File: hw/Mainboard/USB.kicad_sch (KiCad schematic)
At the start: 8 parts, among them J25 USB2.0_HOST_TYPE_C

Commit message: hw: 25x2 header (wip)
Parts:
- renumbered J25 to J26
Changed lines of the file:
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@@
   (symbol (lib_id "PET:PD_GND") (at 102.87 88.9 0) (unit 1)
     (in_bom yes) (on_board yes) (fields_autoplaced)
-    (property "Reference" "#PWR0150" (id 0) (at 102.87 95.25 0)
+    (property "Reference" "#PWR0152" (id 0) (at 102.87 95.25 0)
       (effects (font (size 1.27 1.27)) hide)
     )
@@
   (symbol (lib_id "JLCPCB:USB_C_Receptacle_USB2.0") (at 152.4 92.71 0) (mirror y) (unit 1)
     (in_bom yes) (on_board yes) (fields_autoplaced)
-    (property "Reference" "J25" (id 0) (at 163.83 90.8049 0)
+    (property "Reference" "J26" (id 0) (at 163.83 90.8049 0)
       (effects (font (size 1.27 1.27)) (justify right))
     )
@@
   (symbol (lib_id "power:+5V") (at 102.87 74.93 0) (mirror y) (unit 1)
     (in_bom yes) (on_board yes) (fields_autoplaced)
-    (property "Reference" "#PWR0149" (id 0) (at 102.87 78.74 0)
+    (property "Reference" "#PWR0151" (id 0) (at 102.87 78.74 0)
       (effects (font (size 1.27 1.27)) hide)
     )
@@
   (symbol (lib_id "PET:PD_GND") (at 153.67 123.19 0) (unit 1)
     (in_bom yes) (on_board yes) (fields_autoplaced)
-    (property "Reference" "#PWR0151" (id 0) (at 153.67 129.54 0)
+    (property "Reference" "#PWR0153" (id 0) (at 153.67 129.54 0)
       (effects (font (size 1.27 1.27)) hide)
     )
@@
   (symbol (lib_id "power:GND") (at 160.02 123.19 0) (unit 1)
     (in_bom yes) (on_board yes) (fields_autoplaced)
-    (property "Reference" "#PWR0152" (id 0) (at 160.02 129.54 0)
+    (property "Reference" "#PWR0154" (id 0) (at 160.02 129.54 0)
       (effects (font (size 1.27 1.27)) hide)
     )

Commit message: hw: 2x config switch (wip)
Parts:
- renumbered J26 to J25
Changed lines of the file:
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@@
   (symbol (lib_id "PET:PD_GND") (at 102.87 88.9 0) (unit 1)
     (in_bom yes) (on_board yes) (fields_autoplaced)
-    (property "Reference" "#PWR0152" (id 0) (at 102.87 95.25 0)
+    (property "Reference" "#PWR0158" (id 0) (at 102.87 95.25 0)
       (effects (font (size 1.27 1.27)) hide)
     )
@@
   (symbol (lib_id "JLCPCB:USB_C_Receptacle_USB2.0") (at 152.4 92.71 0) (mirror y) (unit 1)
     (in_bom yes) (on_board yes) (fields_autoplaced)
-    (property "Reference" "J26" (id 0) (at 163.83 90.8049 0)
+    (property "Reference" "J25" (id 0) (at 163.83 90.8049 0)
       (effects (font (size 1.27 1.27)) (justify right))
     )
@@
   (symbol (lib_id "power:+5V") (at 102.87 74.93 0) (mirror y) (unit 1)
     (in_bom yes) (on_board yes) (fields_autoplaced)
-    (property "Reference" "#PWR0151" (id 0) (at 102.87 78.74 0)
+    (property "Reference" "#PWR0157" (id 0) (at 102.87 78.74 0)
       (effects (font (size 1.27 1.27)) hide)
     )
@@
   (symbol (lib_id "PET:PD_GND") (at 153.67 123.19 0) (unit 1)
     (in_bom yes) (on_board yes) (fields_autoplaced)
-    (property "Reference" "#PWR0153" (id 0) (at 153.67 129.54 0)
+    (property "Reference" "#PWR0159" (id 0) (at 153.67 129.54 0)
       (effects (font (size 1.27 1.27)) hide)
     )
@@
   (symbol (lib_id "power:GND") (at 160.02 123.19 0) (unit 1)
     (in_bom yes) (on_board yes) (fields_autoplaced)
-    (property "Reference" "#PWR0154" (id 0) (at 160.02 129.54 0)
+    (property "Reference" "#PWR0160" (id 0) (at 160.02 129.54 0)
       (effects (font (size 1.27 1.27)) hide)
     )

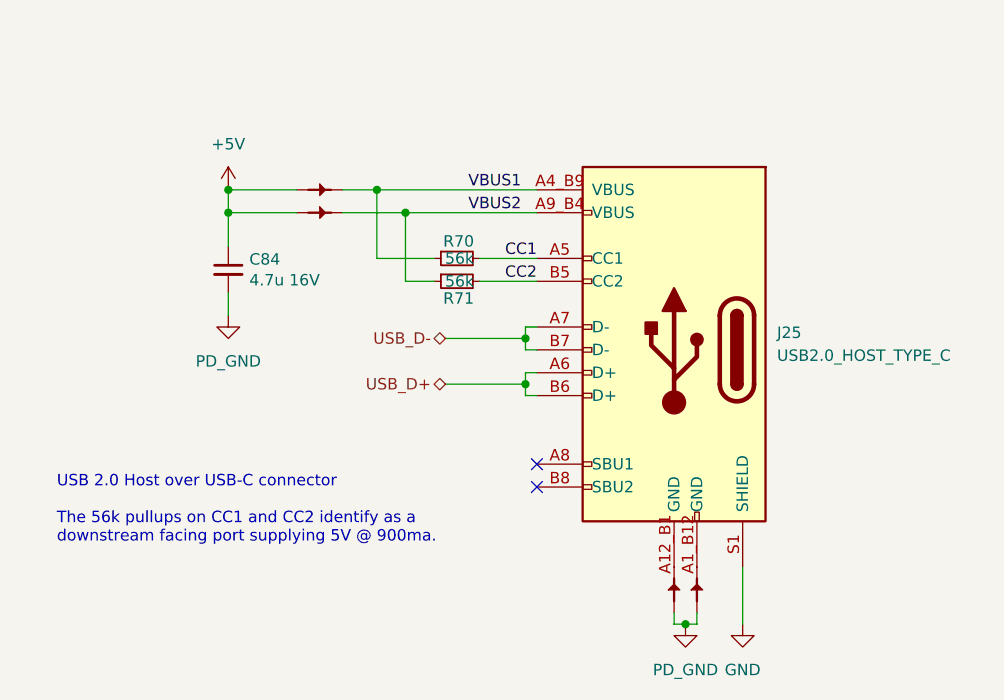
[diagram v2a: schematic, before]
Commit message: hw: add vbus diode, just starting fills
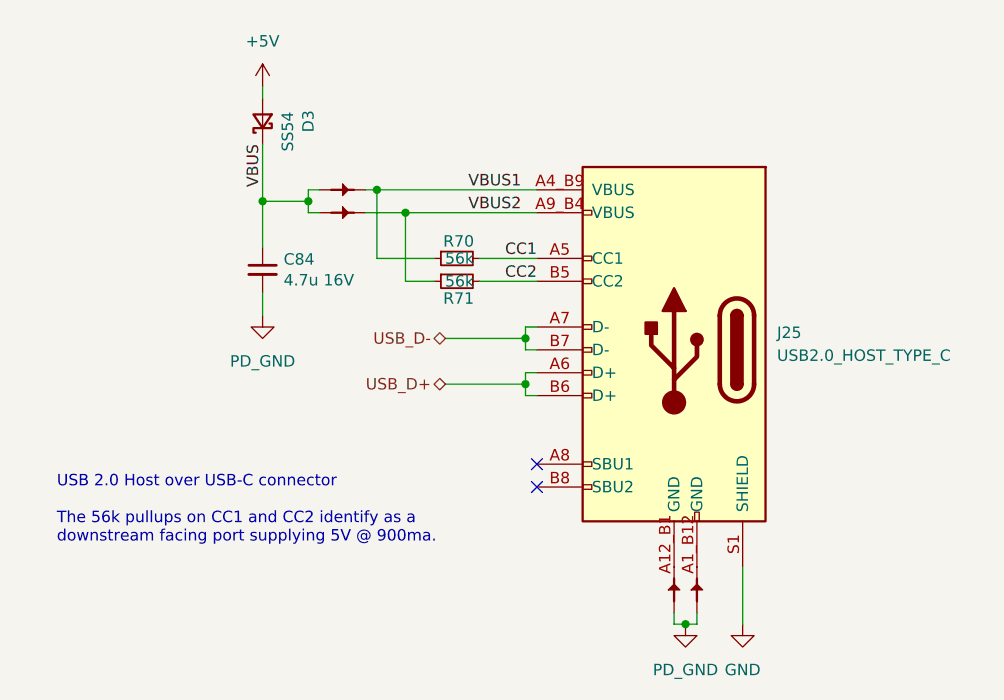
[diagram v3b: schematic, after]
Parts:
- added D3: SS54, Diode_SMD:D_SMA, symbol Device:D_Schottky_Small
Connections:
- net +5V: now also D3.2 (A); no longer C84.1, PT51.1, PT52.1
- new net VBUS: C84.1, D3.1 (K), PT51.1, PT52.1
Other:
- moved on the sheet: C84

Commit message: hw: remove series termination, gnd under hdmi (wip)
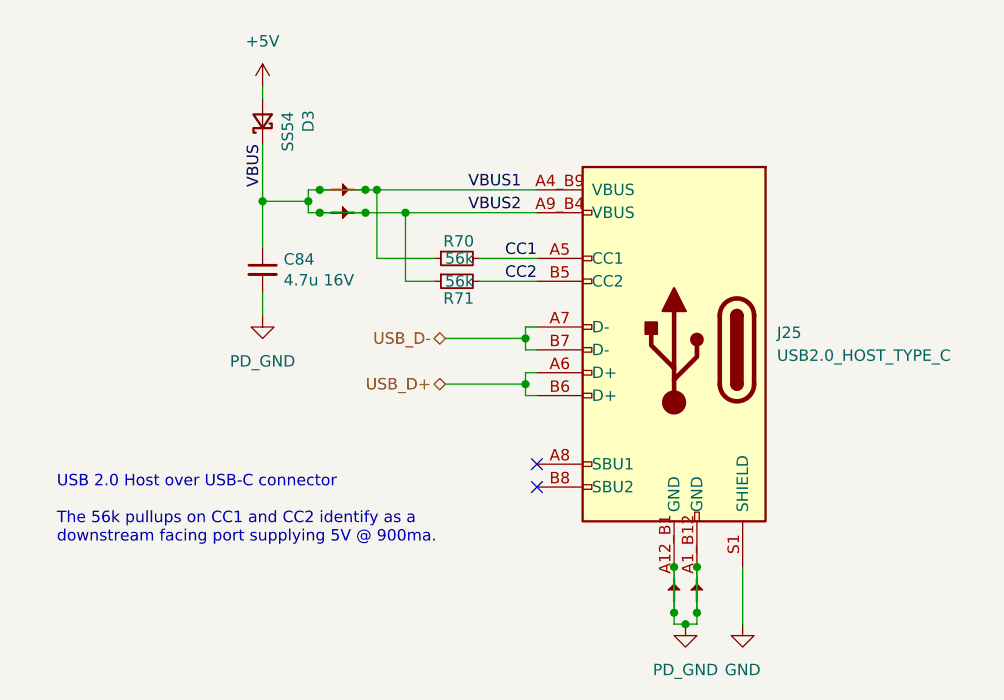
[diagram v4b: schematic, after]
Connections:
- net VBUS1 is gone; now on net VBUS: J25.A4_B9 (VBUS), PT51.2, R70.1
- net VBUS2 is gone; now on net VBUS: J25.A9_B4 (VBUS), PT52.2, R71.1
- net PD_GND: now also J25.A12_B1 (GND), J25.A1_B12 (GND), PT53.2, PT54.2
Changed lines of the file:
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@@
     (title "CBM PET Mainboard Replacement")
   )
+  (junction (at 152.4 116.84) (diameter 0) (color 0 0 0 0)
+  )
+  (junction (at 118.11 74.93) (diameter 0) (color 0 0 0 0)
+  )
+  (junction (at 152.4 121.92) (diameter 0) (color 0 0 0 0)
+  )
   (junction (at 153.67 123.19) (diameter 0) (color 0 0 0 0)
+  )
+  (junction (at 118.11 77.47) (diameter 0) (color 0 0 0 0)
+  )
+  (junction (at 154.94 116.84) (diameter 0) (color 0 0 0 0)
   )
   (junction (at 135.89 96.52) (diameter 0) (color 0 0 0 0)
@@
   (junction (at 135.89 91.44) (diameter 0) (color 0 0 0 0)
   )
+  (junction (at 113.03 74.93) (diameter 0) (color 0 0 0 0)
+  )
+  (junction (at 154.94 121.92) (diameter 0) (color 0 0 0 0)
+  )
   (junction (at 122.555 77.47) (diameter 0) (color 0 0 0 0)
+  )
+  (junction (at 113.03 77.47) (diameter 0) (color 0 0 0 0)
   )
   (no_connect (at 137.16 105.41))
@@
     (stroke (width 0) (type default) (color 0 0 0 0))
   )
+  (wire (pts (xy 154.94 116.84) (xy 154.94 121.92))
+    (stroke (width 0) (type default) (color 0 0 0 0))
+  )
   (wire (pts (xy 152.4 121.92) (xy 152.4 123.19))
     (stroke (width 0) (type default) (color 0 0 0 0))
@@
     (stroke (width 0) (type default) (color 0 0 0 0))
   )
+  (wire (pts (xy 113.03 77.47) (xy 118.11 77.47))
+    (stroke (width 0) (type default) (color 0 0 0 0))
+  )
   (wire (pts (xy 118.11 77.47) (xy 122.555 77.47))
     (stroke (width 0) (type default) (color 0 0 0 0))
   )
   (wire (pts (xy 119.38 74.93) (xy 137.16 74.93))
+    (stroke (width 0) (type default) (color 0 0 0 0))
+  )
+  (wire (pts (xy 113.03 74.93) (xy 118.11 74.93))
     (stroke (width 0) (type default) (color 0 0 0 0))
   )
@@
     (stroke (width 0) (type default) (color 0 0 0 0))
   )
+  (wire (pts (xy 152.4 116.84) (xy 152.4 121.92))
+    (stroke (width 0) (type default) (color 0 0 0 0))
+  )

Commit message: hw: caps & logos (wip)
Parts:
- added C101: 47u 10V, Capacitor_SMD:C_1206_3216Metric, symbol Device:C_Small
- C84: value 4.7u 16V -> 1u; footprint Capacitor_SMD:C_0603_1608Metric -> Capacitor_SMD:C_0402_1005Metric; LCSC C19666 -> C52923
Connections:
- net PD_GND: now also C101.2
- net VBUS: now also C101.1
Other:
- title: CBM PET Mainboard Replacement -> EconoPET 40/8096
- moved on the sheet: D3

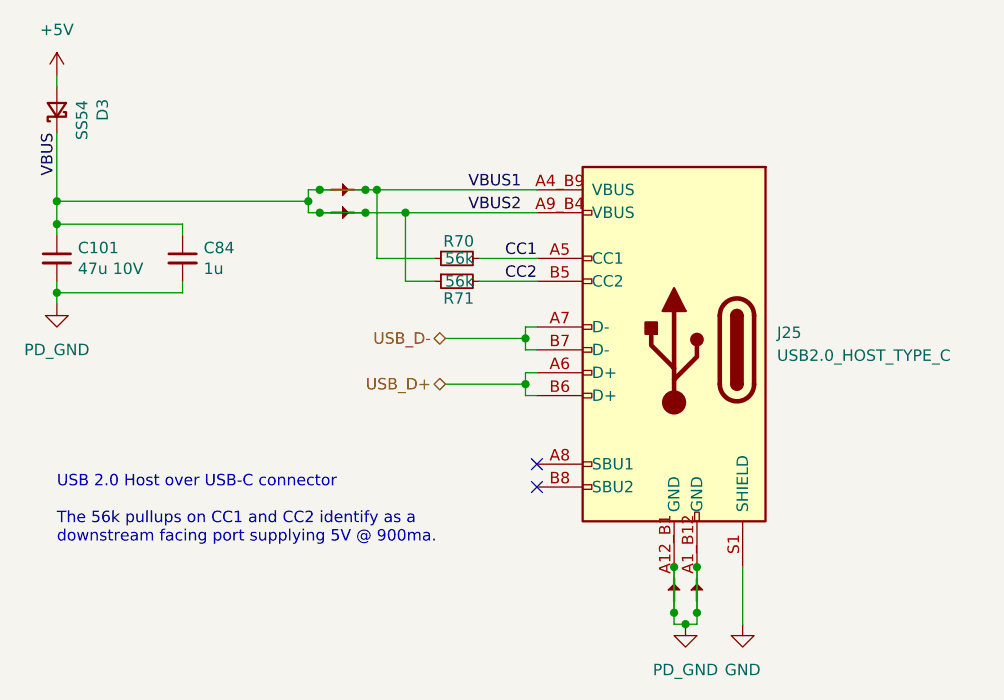
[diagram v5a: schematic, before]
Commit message: hw: remove net/power ties
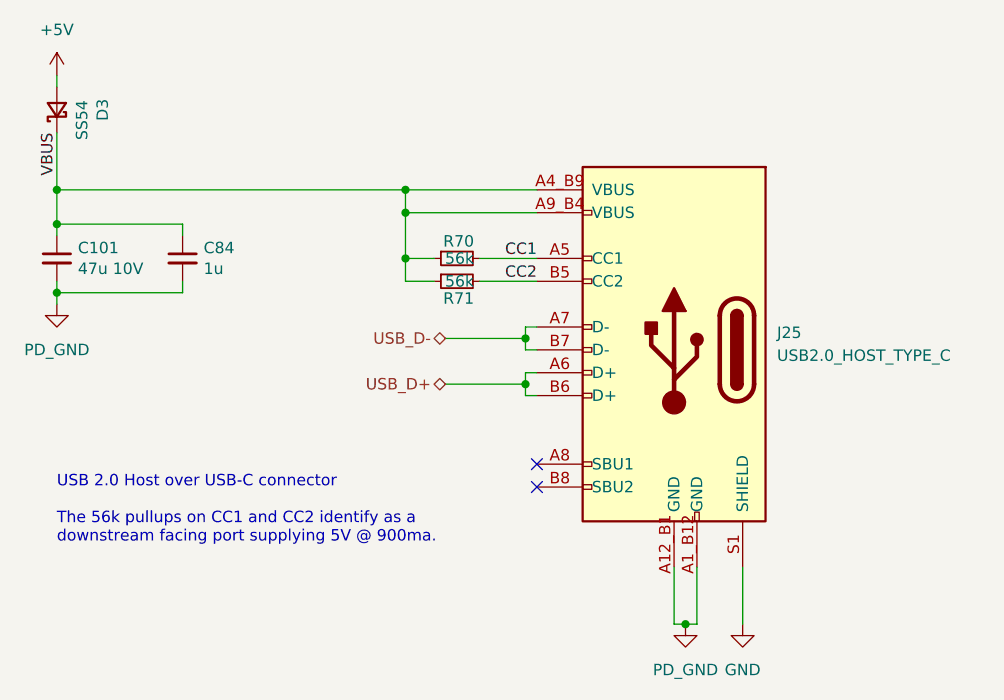
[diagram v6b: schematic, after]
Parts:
- removed PT51, PT52, PT53, PT54: PowerTie_2, PET:NetTie-2_SMD_Pad_1.6_to_0.4mm, symbol PET:PowerTie_2
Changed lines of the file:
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@@
     (rev "A")
   )
-  (junction (at 152.4 116.84) (diameter 0) (color 0 0 0 0)
-  )
-  (junction (at 118.11 74.93) (diameter 0) (color 0 0 0 0)
-  )
-  (junction (at 152.4 121.92) (diameter 0) (color 0 0 0 0)
-  )
   (junction (at 153.67 123.19) (diameter 0) (color 0 0 0 0)
   )
-  (junction (at 118.11 77.47) (diameter 0) (color 0 0 0 0)
+  (junction (at 122.555 77.47) (diameter 0) (color 0 0 0 0)
   )
   (junction (at 83.82 78.74) (diameter 0) (color 0 0 0 0)
   )
-  (junction (at 154.94 116.84) (diameter 0) (color 0 0 0 0)
+  (junction (at 83.82 74.93) (diameter 0) (color 0 0 0 0)
   )
   (junction (at 83.82 86.36) (diameter 0) (color 0 0 0 0)
@@
   (junction (at 135.89 96.52) (diameter 0) (color 0 0 0 0)
   )
-  (junction (at 119.38 74.93) (diameter 0) (color 0 0 0 0)
-  )
-  (junction (at 111.76 76.2) (diameter 0) (color 0 0 0 0)
-  )
   (junction (at 135.89 91.44) (diameter 0) (color 0 0 0 0)
   )
-  (junction (at 113.03 74.93) (diameter 0) (color 0 0 0 0)
-  )
-  (junction (at 83.82 76.2) (diameter 0) (color 0 0 0 0)
-  )
-  (junction (at 154.94 121.92) (diameter 0) (color 0 0 0 0)
-  )
-  (junction (at 122.555 77.47) (diameter 0) (color 0 0 0 0)
-  )
-  (junction (at 113.03 77.47) (diameter 0) (color 0 0 0 0)
+  (junction (at 122.555 82.55) (diameter 0) (color 0 0 0 0)
+  )
+  (junction (at 122.555 74.93) (diameter 0) (color 0 0 0 0)
   )
   (no_connect (at 137.16 105.41))
   (no_connect (at 137.16 107.95))
+  (wire (pts (xy 83.82 74.93) (xy 83.82 78.74))
+    (stroke (width 0) (type default) (color 0 0 0 0))
+  )
   (wire (pts (xy 83.82 78.74) (xy 97.79 78.74))
     (stroke (width 0) (type default) (color 0 0 0 0))
@@
     (stroke (width 0) (type default) (color 0 0 0 0))
   )
-  (wire (pts (xy 119.38 82.55) (xy 119.38 74.93))
-    (stroke (width 0) (type default) (color 0 0 0 0))
-  )
   (wire (pts (xy 122.555 77.47) (xy 137.16 77.47))
     (stroke (width 0) (type default) (color 0 0 0 0))
   )
-  (wire (pts (xy 83.82 68.58) (xy 83.82 76.2))
+  (wire (pts (xy 83.82 68.58) (xy 83.82 74.93))
     (stroke (width 0) (type default) (color 0 0 0 0))
   )
@@
     (stroke (width 0) (type default) (color 0 0 0 0))
   )
-  (wire (pts (xy 125.73 82.55) (xy 119.38 82.55))
-    (stroke (width 0) (type default) (color 0 0 0 0))
-  )
   (wire (pts (xy 83.82 62.23) (xy 83.82 63.5))
     (stroke (width 0) (type default) (color 0 0 0 0))
@@
     (stroke (width 0) (type default) (color 0 0 0 0))
   )
-  (wire (pts (xy 154.94 116.84) (xy 154.94 121.92))
-    (stroke (width 0) (type default) (color 0 0 0 0))
-  )
-  (wire (pts (xy 152.4 121.92) (xy 152.4 123.19))
+  (wire (pts (xy 154.94 116.84) (xy 154.94 123.19))
+    (stroke (width 0) (type default) (color 0 0 0 0))
+  )
+  (wire (pts (xy 122.555 82.55) (xy 122.555 77.47))
     (stroke (width 0) (type default) (color 0 0 0 0))
   )
@@
     (stroke (width 0) (type default) (color 0 0 0 0))
   )
-  (wire (pts (xy 113.03 74.93) (xy 111.76 74.93))
+  (wire (pts (xy 83.82 74.93) (xy 122.555 74.93))
     (stroke (width 0) (type default) (color 0 0 0 0))
   )
@@
     (stroke (width 0) (type default) (color 0 0 0 0))
   )
-  (wire (pts (xy 122.555 85.09) (xy 122.555 77.47))
-    (stroke (width 0) (type default) (color 0 0 0 0))
-  )
-  (wire (pts (xy 113.03 77.47) (xy 118.11 77.47))
-    (stroke (width 0) (type default) (color 0 0 0 0))
-  )
-  (wire (pts (xy 118.11 77.47) (xy 122.555 77.47))
-    (stroke (width 0) (type default) (color 0 0 0 0))
-  )
-  (wire (pts (xy 119.38 74.93) (xy 137.16 74.93))
-    (stroke (width 0) (type default) (color 0 0 0 0))
-  )
-  (wire (pts (xy 113.03 74.93) (xy 118.11 74.93))
-    (stroke (width 0) (type default) (color 0 0 0 0))
-  )
-  (wire (pts (xy 111.76 77.47) (xy 113.03 77.47))
+  (wire (pts (xy 122.555 85.09) (xy 122.555 82.55))
+    (stroke (width 0) (type default) (color 0 0 0 0))
+  )
+  (wire (pts (xy 122.555 82.55) (xy 125.73 82.55))
     (stroke (width 0) (type default) (color 0 0 0 0))
   )
@@
     (stroke (width 0) (type default) (color 0 0 0 0))
   )
-  (wire (pts (xy 83.82 76.2) (xy 83.82 78.74))
-    (stroke (width 0) (type default) (color 0 0 0 0))
-  )
-  (wire (pts (xy 111.76 76.2) (xy 111.76 77.47))
-    (stroke (width 0) (type default) (color 0 0 0 0))
-  )
   (wire (pts (xy 135.89 96.52) (xy 127 96.52))
     (stroke (width 0) (type default) (color 0 0 0 0))
@@
     (stroke (width 0) (type default) (color 0 0 0 0))
   )
-  (wire (pts (xy 152.4 116.84) (xy 152.4 121.92))
+  (wire (pts (xy 122.555 77.47) (xy 122.555 74.93))
+    (stroke (width 0) (type default) (color 0 0 0 0))
+  )
+  (wire (pts (xy 152.4 116.84) (xy 152.4 123.19))
     (stroke (width 0) (type default) (color 0 0 0 0))
   )
@@
     (stroke (width 0) (type default) (color 0 0 0 0))
   )
-  (wire (pts (xy 154.94 121.92) (xy 154.94 123.19))
-    (stroke (width 0) (type default) (color 0 0 0 0))
-  )
   (wire (pts (xy 135.89 95.25) (xy 135.89 96.52))
     (stroke (width 0) (type default) (color 0 0 0 0))
@@
     (stroke (width 0) (type default) (color 0 0 0 0))
   )
+  (wire (pts (xy 122.555 74.93) (xy 137.16 74.93))
+    (stroke (width 0) (type default) (color 0 0 0 0))
+  )
   (wire (pts (xy 153.67 123.19) (xy 154.94 123.19))
     (stroke (width 0) (type default) (color 0 0 0 0))
   )
-  (wire (pts (xy 111.76 74.93) (xy 111.76 76.2))
-    (stroke (width 0) (type default) (color 0 0 0 0))
-  )
-  (wire (pts (xy 83.82 76.2) (xy 111.76 76.2))
-    (stroke (width 0) (type default) (color 0 0 0 0))
-  )
   (wire (pts (xy 135.89 91.44) (xy 135.89 92.71))
     (stroke (width 0) (type default) (color 0 0 0 0))
   )
   (wire (pts (xy 97.79 80.01) (xy 97.79 78.74))
-    (stroke (width 0) (type default) (color 0 0 0 0))
-  )
-  (wire (pts (xy 118.11 74.93) (xy 119.38 74.93))
     (stroke (width 0) (type default) (color 0 0 0 0))
   )
@@
     (effects (font (size 1.27 1.27)) (justify left bottom))
   )
-  (label "VBUS2" (at 129.54 77.47 0)
-    (effects (font (size 1.27 1.27)) (justify left bottom))
-  )
   (label "VBUS" (at 83.82 68.58 270)
     (effects (font (size 1.27 1.27)) (justify right bottom))
@@
   (label "CC2" (at 137.16 85.09 180)
     (effects (font (size 1.27 1.27)) (justify right bottom))
-  )
-  (label "VBUS1" (at 129.54 74.93 0)
-    (effects (font (size 1.27 1.27)) (justify left bottom))
   )
   (label "CC1" (at 137.16 82.55 180)
@@
     )
     (pin "1")
-  )
-  (symbol (lib_id "PET:PowerTie_2") (at 115.57 74.93 0) (unit 1)
-    (in_bom yes) (on_board yes) (fields_autoplaced)
-    (property "Reference" "PT51" (id 0) (at 115.57 73.025 0)
-      (effects (font (size 1.27 1.27)) hide)
-    )
-    (property "Value" "PowerTie_2" (id 1) (at 115.57 76.835 0)
-      (effects (font (size 1.27 1.27)) hide)
-    )
-    (property "Footprint" "PET:NetTie-2_SMD_Pad_1.6_to_0.4mm" (id 2) (at 115.57 74.93 0)
-      (effects (font (size 1.27 1.27)) hide)
-    )
-    (property "Datasheet" "~" (id 3) (at 115.57 74.93 0)
-      (effects (font (size 1.27 1.27)) hide)
-    )
-    (pin "1")
-    (pin "2")
   )
   (symbol (lib_id "JLCPCB:USB_C_Receptacle_USB2.0") (at 152.4 92.71 0) (mirror y) (unit 1)
@@
     (pin "S1")
   )
-  (symbol (lib_id "PET:PowerTie_2") (at 154.94 119.38 90) (unit 1)
-    (in_bom yes) (on_board yes) (fields_autoplaced)
-    (property "Reference" "PT54" (id 0) (at 153.035 119.38 0)
-      (effects (font (size 1.27 1.27)) hide)
-    )
-    (property "Value" "PowerTie_2" (id 1) (at 156.845 119.38 0)
-      (effects (font (size 1.27 1.27)) hide)
-    )
-    (property "Footprint" "PET:NetTie-2_SMD_Pad_1.6_to_0.4mm" (id 2) (at 154.94 119.38 0)
-      (effects (font (size 1.27 1.27)) hide)
-    )
-    (property "Datasheet" "~" (id 3) (at 154.94 119.38 0)
-      (effects (font (size 1.27 1.27)) hide)
-    )
-    (pin "1")
-    (pin "2")
-  )
   (symbol (lib_id "Device:D_Schottky_Small") (at 83.82 66.04 90) (unit 1)
     (in_bom yes) (on_board yes)
@@
     (pin "2")
   )
-  (symbol (lib_id "PET:PowerTie_2") (at 152.4 119.38 90) (unit 1)
-    (in_bom yes) (on_board yes) (fields_autoplaced)
-    (property "Reference" "PT53" (id 0) (at 150.495 119.38 0)
-      (effects (font (size 1.27 1.27)) hide)
-    )
-    (property "Value" "PowerTie_2" (id 1) (at 154.305 119.38 0)
-      (effects (font (size 1.27 1.27)) hide)
-    )
-    (property "Footprint" "PET:NetTie-2_SMD_Pad_1.6_to_0.4mm" (id 2) (at 152.4 119.38 0)
-      (effects (font (size 1.27 1.27)) hide)
-    )
-    (property "Datasheet" "~" (id 3) (at 152.4 119.38 0)
-      (effects (font (size 1.27 1.27)) hide)
-    )
-    (pin "1")
-    (pin "2")
-  )
   (symbol (lib_id "power:+5V") (at 83.82 62.23 0) (mirror y) (unit 1)
     (in_bom yes) (on_board yes) (fields_autoplaced)
@@
     (pin "1")
   )
-  (symbol (lib_id "PET:PowerTie_2") (at 115.57 77.47 0) (unit 1)
-    (in_bom yes) (on_board yes) (fields_autoplaced)
-    (property "Reference" "PT52" (id 0) (at 115.57 75.565 0)
-      (effects (font (size 1.27 1.27)) hide)
-    )
-    (property "Value" "PowerTie_2" (id 1) (at 115.57 79.375 0)
-      (effects (font (size 1.27 1.27)) hide)
-    )
-    (property "Footprint" "PET:NetTie-2_SMD_Pad_1.6_to_0.4mm" (id 2) (at 115.57 77.47 0)
-      (effects (font (size 1.27 1.27)) hide)
-    )
-    (property "Datasheet" "~" (id 3) (at 115.57 77.47 0)
-      (effects (font (size 1.27 1.27)) hide)
-    )
-    (pin "1")
-    (pin "2")
-  )
   (symbol (lib_id "power:GND") (at 160.02 123.19 0) (unit 1)
